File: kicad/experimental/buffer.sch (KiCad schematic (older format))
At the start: 25 parts

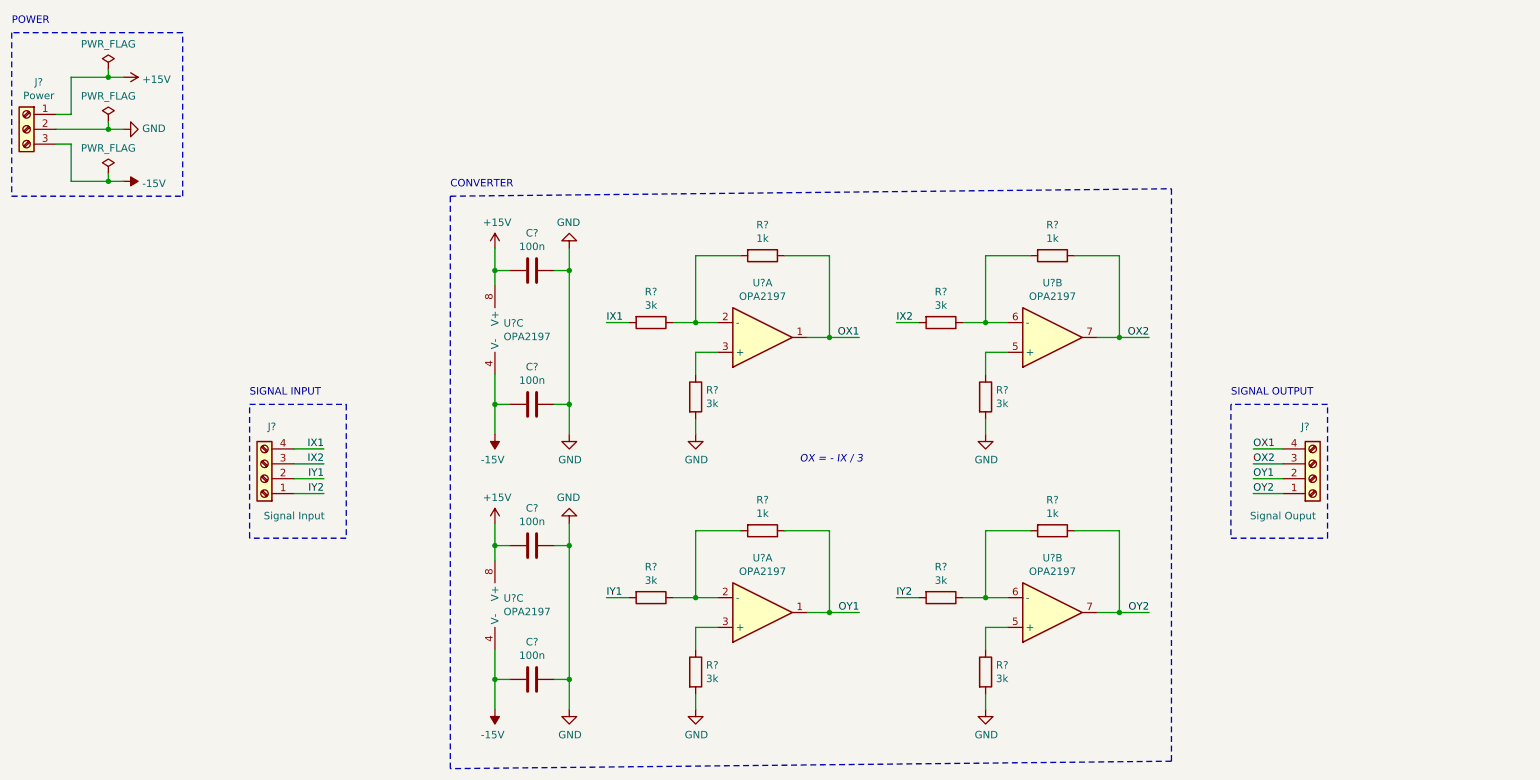
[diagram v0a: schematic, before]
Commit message: created schematic for experimental adc
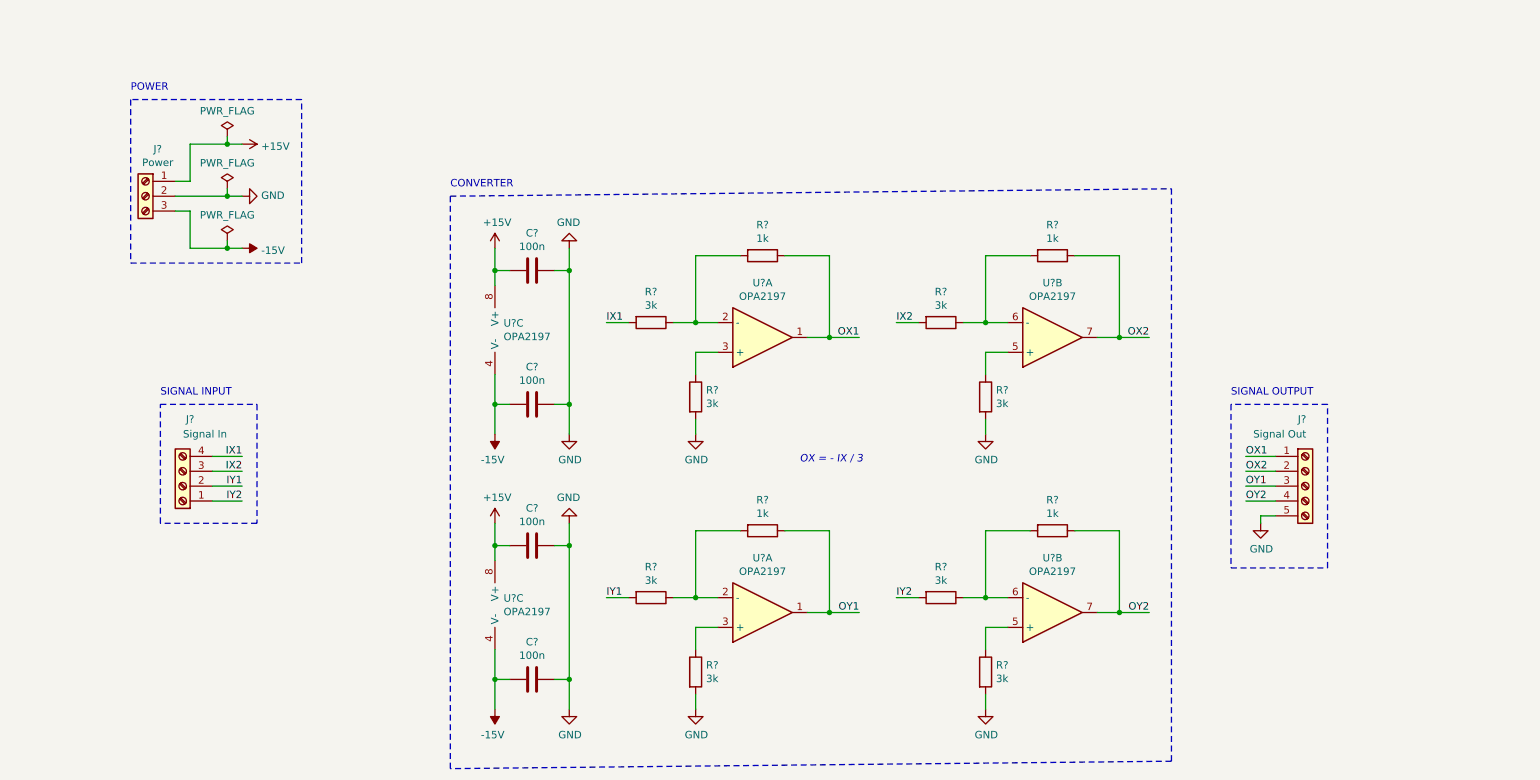
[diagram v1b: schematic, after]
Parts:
- removed J?: Signal Ouput, symbol Connector:Screw_Terminal_01x04
- added J?: Signal Out, symbol Connector:Screw_Terminal_01x05
- J?: value Signal Input -> Signal In
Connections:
- net GND: now also J?.5 (Pin_5)
- net OX1: now also J?.1 (Pin_1)
- net OX2: now also J?.2 (Pin_2)
- net OY1: now also J?.3 (Pin_3)
- net OY2: now also J?.4 (Pin_4)
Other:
- moved on the sheet: J?
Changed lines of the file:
@@
 L Connector:Screw_Terminal_01x03 J?
 U 1 1 5D6252EA
-P 850 1400
-F 0 "J?" H 768 1717 50  0000 C CNN
-F 1 "Power" H 768 1626 50  0000 C CNN
-F 2 "" H 850 1400 50  0001 C CNN
-F 3 "~" H 850 1400 50  0001 C CNN
-	1    850  1400
+P 1650 1850
+F 0 "J?" H 1568 2167 50  0000 C CNN
+F 1 "Power" H 1568 2076 50  0000 C CNN
+F 2 "" H 1650 1850 50  0001 C CNN
+F 3 "~" H 1650 1850 50  0001 C CNN
+	1    1650 1850
 	-1   0    0    -1
 $EndComp
@@
 L power:+15V #PWR?
 U 1 1 5D627080
-P 1500 1050
-F 0 "#PWR?" H 1500 900 50  0001 C CNN
-F 1 "+15V" V 1515 1178 50  0000 L CNN
-F 2 "" H 1500 1050 50  0001 C CNN
-F 3 "" H 1500 1050 50  0001 C CNN
-	1    1500 1050
-	0    1    1    0
-$EndComp
-Wire Wire Line
-	1500 1050 1400 1050
-Wire Wire Line
-	1150 1050 1150 1300
-Wire Wire Line
-	1150 1300 1050 1300
+P 2300 1500
+F 0 "#PWR?" H 2300 1350 50  0001 C CNN
+F 1 "+15V" V 2315 1628 50  0000 L CNN
+F 2 "" H 2300 1500 50  0001 C CNN
+F 3 "" H 2300 1500 50  0001 C CNN
+	1    2300 1500
+	0    1    1    0
+$EndComp
+Wire Wire Line
+	2300 1500 2200 1500
+Wire Wire Line
+	1950 1500 1950 1750
+Wire Wire Line
+	1950 1750 1850 1750
 $Comp
 L power:-15V #PWR?
 U 1 1 5D627AC9
-P 1500 1750
-F 0 "#PWR?" H 1500 1850 50  0001 C CNN
-F 1 "-15V" V 1515 1878 50  0000 L CNN
-F 2 "" H 1500 1750 50  0001 C CNN
-F 3 "" H 1500 1750 50  0001 C CNN
-	1    1500 1750
-	0    1    1    0
-$EndComp
-Wire Wire Line
-	1500 1750 1400 1750
-Wire Wire Line
-	1150 1750 1150 1500
-Wire Wire Line
-	1150 1500 1050 1500
+P 2300 2200
+F 0 "#PWR?" H 2300 2300 50  0001 C CNN
+F 1 "-15V" V 2315 2328 50  0000 L CNN
+F 2 "" H 2300 2200 50  0001 C CNN
+F 3 "" H 2300 2200 50  0001 C CNN
+	1    2300 2200
+	0    1    1    0
+$EndComp
+Wire Wire Line
+	2300 2200 2200 2200
+Wire Wire Line
+	1950 2200 1950 1950
+Wire Wire Line
+	1950 1950 1850 1950
 $Comp
 L power:GND #PWR?
 U 1 1 5D628485
-P 1500 1400
-F 0 "#PWR?" H 1500 1150 50  0001 C CNN
-F 1 "GND" V 1505 1272 50  0000 R CNN
-F 2 "" H 1500 1400 50  0001 C CNN
-F 3 "" H 1500 1400 50  0001 C CNN
-	1    1500 1400
+P 2300 1850
+F 0 "#PWR?" H 2300 1600 50  0001 C CNN
+F 1 "GND" V 2305 1722 50  0000 R CNN
+F 2 "" H 2300 1850 50  0001 C CNN
+F 3 "" H 2300 1850 50  0001 C CNN
+	1    2300 1850
 	0    -1   -1   0
 $EndComp
 Wire Wire Line
-	1500 1400 1400 1400
+	2300 1850 2200 1850
 $Comp
 L power:PWR_FLAG #FLG?
 U 1 1 5D628CB7
-P 1400 1000
-F 0 "#FLG?" H 1400 1075 50  0001 C CNN
-F 1 "PWR_FLAG" H 1400 1173 50  0000 C CNN
-F 2 "" H 1400 1000 50  0001 C CNN
-F 3 "~" H 1400 1000 50  0001 C CNN
-	1    1400 1000
-	1    0    0    -1
-$EndComp
-Wire Wire Line
-	1400 1000 1400 1050
-Connection ~ 1400 1050
-Wire Wire Line
-	1400 1050 1150 1050
+P 2200 1450
+F 0 "#FLG?" H 2200 1525 50  0001 C CNN
+F 1 "PWR_FLAG" H 2200 1623 50  0000 C CNN
+F 2 "" H 2200 1450 50  0001 C CNN
+F 3 "~" H 2200 1450 50  0001 C CNN
+	1    2200 1450
+	1    0    0    -1
+$EndComp
+Wire Wire Line
+	2200 1450 2200 1500
+Connection ~ 2200 1500
+Wire Wire Line
+	2200 1500 1950 1500
 $Comp
 L power:PWR_FLAG #FLG?
 U 1 1 5D62989E
-P 1400 1350
-F 0 "#FLG?" H 1400 1425 50  0001 C CNN
-F 1 "PWR_FLAG" H 1400 1523 50  0000 C CNN
-F 2 "" H 1400 1350 50  0001 C CNN
-F 3 "~" H 1400 1350 50  0001 C CNN
-	1    1400 1350
-	1    0    0    -1
-$EndComp
-Wire Wire Line
-	1400 1350 1400 1400
-Connection ~ 1400 1400
-Wire Wire Line
-	1400 1400 1050 1400
+P 2200 1800
+F 0 "#FLG?" H 2200 1875 50  0001 C CNN
+F 1 "PWR_FLAG" H 2200 1973 50  0000 C CNN
+F 2 "" H 2200 1800 50  0001 C CNN
+F 3 "~" H 2200 1800 50  0001 C CNN
+	1    2200 1800
+	1    0    0    -1
+$EndComp
+Wire Wire Line
+	2200 1800 2200 1850
+Connection ~ 2200 1850
+Wire Wire Line
+	2200 1850 1850 1850
 $Comp
 L power:PWR_FLAG #FLG?
 U 1 1 5D629BA8
-P 1400 1700
-F 0 "#FLG?" H 1400 1775 50  0001 C CNN
-F 1 "PWR_FLAG" H 1400 1873 50  0000 C CNN
-F 2 "" H 1400 1700 50  0001 C CNN
-F 3 "~" H 1400 1700 50  0001 C CNN
-	1    1400 1700
-	1    0    0    -1
-$EndComp
-Wire Wire Line
-	1400 1700 1400 1750
-Connection ~ 1400 1750
-Wire Wire Line
-	1400 1750 1150 1750
-Wire Notes Line
-	750  750  750  1850
-Wire Notes Line
-	750  1850 1900 1850
-Wire Notes Line
-	1900 1850 1900 750
-Wire Notes Line
-	1900 750  750  750
-Text Notes 750  700  0    50   ~ 0
+P 2200 2150
+F 0 "#FLG?" H 2200 2225 50  0001 C CNN
+F 1 "PWR_FLAG" H 2200 2323 50  0000 C CNN
+F 2 "" H 2200 2150 50  0001 C CNN
+F 3 "~" H 2200 2150 50  0001 C CNN
+	1    2200 2150
+	1    0    0    -1
+$EndComp
+Wire Wire Line
+	2200 2150 2200 2200
+Connection ~ 2200 2200
+Wire Wire Line
+	2200 2200 1950 2200
+Wire Notes Line
+	1550 1200 1550 2300
+Wire Notes Line
+	1550 2300 2700 2300
+Wire Notes Line
+	2700 2300 2700 1200
+Wire Notes Line
+	2700 1200 1550 1200
+Text Notes 1550 1150 0    50   ~ 0
 POWER
 $Comp
@@
 L Connector:Screw_Terminal_01x04 J?
 U 1 1 5D62F7ED
-P 2450 3750
-F 0 "J?" H 2400 3400 50  0000 C CNN
-F 1 "Signal Input" H 2250 4000 50  0000 C CNN
-F 2 "" H 2450 3750 50  0001 C CNN
-F 3 "~" H 2450 3750 50  0001 C CNN
-	1    2450 3750
+P 1900 3800
+F 0 "J?" H 1850 3350 50  0000 C CNN
+F 1 "Signal In" H 1750 3450 50  0000 C CNN
+F 2 "" H 1900 3800 50  0001 C CNN
+F 3 "~" H 1900 3800 50  0001 C CNN
+	1    1900 3800
 	-1   0    0    1
 $EndComp
-Text Label 2850 3550 2    50   ~ 0
+Text Label 2300 3600 2    50   ~ 0
 IX1
 Wire Wire Line
-	2850 3550 2650 3550
-Text Label 2850 3650 2    50   ~ 0
+	2300 3600 2100 3600
+Text Label 2300 3700 2    50   ~ 0
 IX2
 Wire Wire Line
-	2850 3650 2650 3650
-Text Label 2850 3750 2    50   ~ 0
+	2300 3700 2100 3700
+Text Label 2300 3800 2    50   ~ 0
 IY1
 Wire Wire Line
-	2850 3750 2650 3750
-Text Label 2850 3850 2    50   ~ 0
+	2300 3800 2100 3800
+Text Label 2300 3900 2    50   ~ 0
 IY2
 Wire Wire Line
-	2850 3850 2650 3850
-Wire Notes Line
-	2350 3250 3000 3250
-Wire Notes Line
-	3000 3250 3000 4150
-Wire Notes Line
-	3000 4150 2350 4150
-Wire Notes Line
-	2350 4150 2350 3250
-Text Notes 2350 3200 0    50   ~ 0
+	2300 3900 2100 3900
+Wire Notes Line
+	1750 3250 2400 3250
+Wire Notes Line
+	2400 3250 2400 4050
+Wire Notes Line
+	2400 4050 1750 4050
+Wire Notes Line
+	1750 4050 1750 3250
+Text Notes 1750 3200 0    50   ~ 0
 SIGNAL INPUT
 $Comp
@@
 Wire Wire Line
 	7150 4550 7300 4550
-$Comp
-L Connector:Screw_Terminal_01x04 J?
-U 1 1 5D6B2A8E
-P 9500 3750
-F 0 "J?" H 9450 3400 50  0000 C CNN
-F 1 "Signal Ouput" H 9300 4000 50  0000 C CNN
-F 2 "" H 9500 3750 50  0001 C CNN
-F 3 "~" H 9500 3750 50  0001 C CNN
-	1    9500 3750
-	1    0    0    1
-$EndComp
-Text Label 9100 3550 0    50   ~ 0
+Text Label 9050 3600 0    50   ~ 0
 OX1
 Wire Wire Line
-	9100 3550 9300 3550
-Text Label 9100 3650 0    50   ~ 0
+	9050 3600 9250 3600
+Text Label 9050 3700 0    50   ~ 0
 OX2
 Wire Wire Line
-	9100 3650 9300 3650
-Text Label 9100 3750 0    50   ~ 0
+	9050 3700 9250 3700
+Text Label 9050 3800 0    50   ~ 0
 OY1
 Wire Wire Line
-	9100 3750 9300 3750
-Text Label 9100 3850 0    50   ~ 0
+	9050 3800 9250 3800
+Text Label 9050 3900 0    50   ~ 0
 OY2
 Wire Wire Line
-	9100 3850 9300 3850
+	9050 3900 9250 3900
 Wire Notes Line
 	9600 3250 8950 3250
 Wire Notes Line
-	8950 3250 8950 4150
-Wire Notes Line
-	8950 4150 9600 4150
-Wire Notes Line
-	9600 4150 9600 3250
+	8950 3250 8950 4350
+Wire Notes Line
+	8950 4350 9600 4350
+Wire Notes Line
+	9600 4350 9600 3250
 Text Notes 8950 3200 0    50   ~ 0
 SIGNAL OUTPUT
 Text Notes 6050 3650 0    50   Italic 0
 OX = - IX / 3
+$Comp
+L Connector:Screw_Terminal_01x05 J?
+U 1 1 5D6D5912
+P 9450 3800
+F 0 "J?" H 9400 4250 50  0000 L CNN
+F 1 "Signal Out" H 9100 4150 50  0000 L CNN
+F 2 "" H 9450 3800 50  0001 C CNN
+F 3 "~" H 9450 3800 50  0001 C CNN
+	1    9450 3800
+	1    0    0    -1
+$EndComp
+$Comp
+L power:GND #PWR?
+U 1 1 5D6E01D6
+P 9150 4050
+F 0 "#PWR?" H 9150 3800 50  0001 C CNN
+F 1 "GND" H 9155 3877 50  0000 C CNN
+F 2 "" H 9150 4050 50  0001 C CNN
+F 3 "" H 9150 4050 50  0001 C CNN
+	1    9150 4050
+	1    0    0    -1
+$EndComp
+Wire Wire Line
+	9150 4050 9150 4000
+Wire Wire Line
+	9150 4000 9250 4000
 $EndSCHEMATC

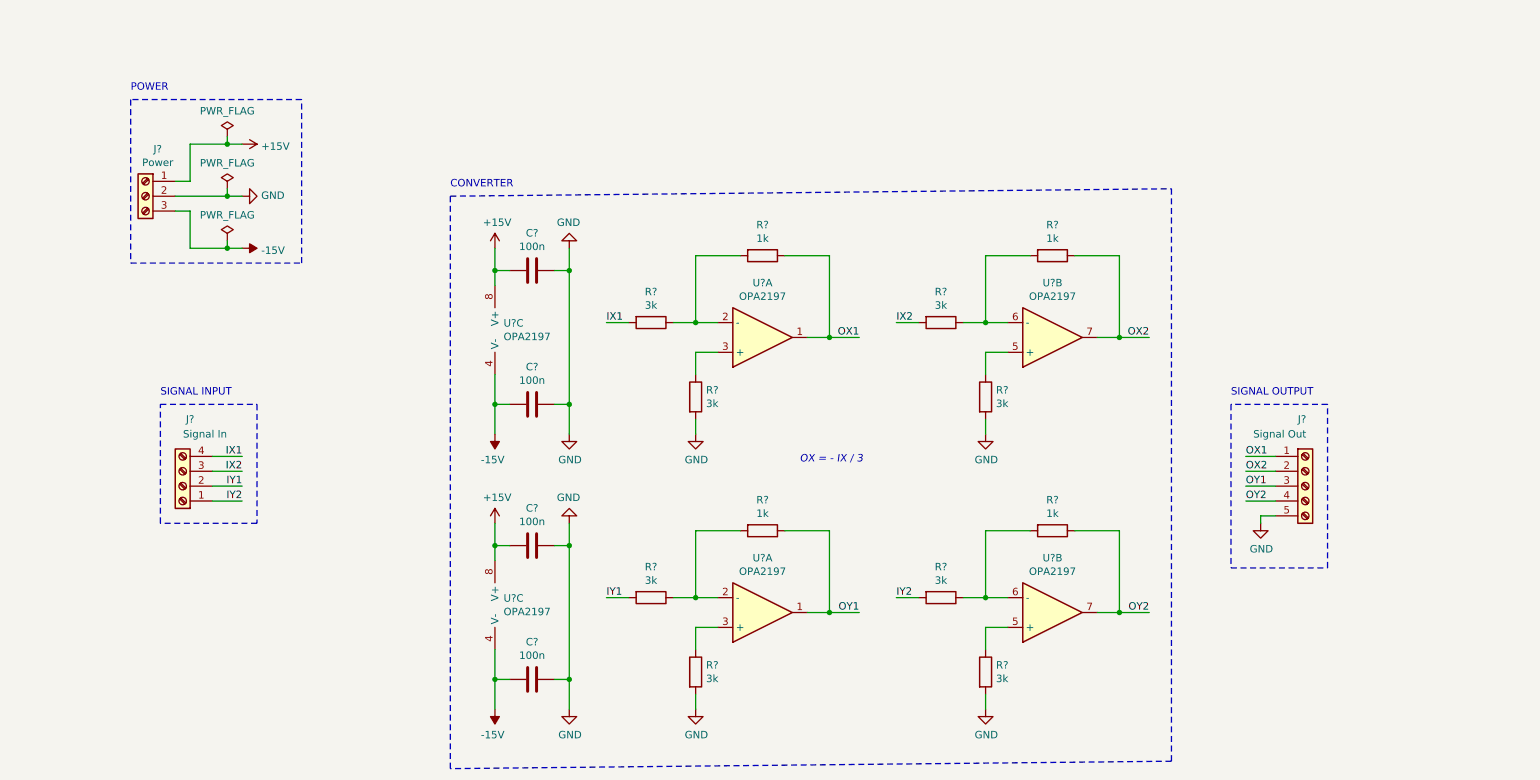
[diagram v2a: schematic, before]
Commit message: added test points to experimental adc and buffer boards, improved schematic, assigned footprints
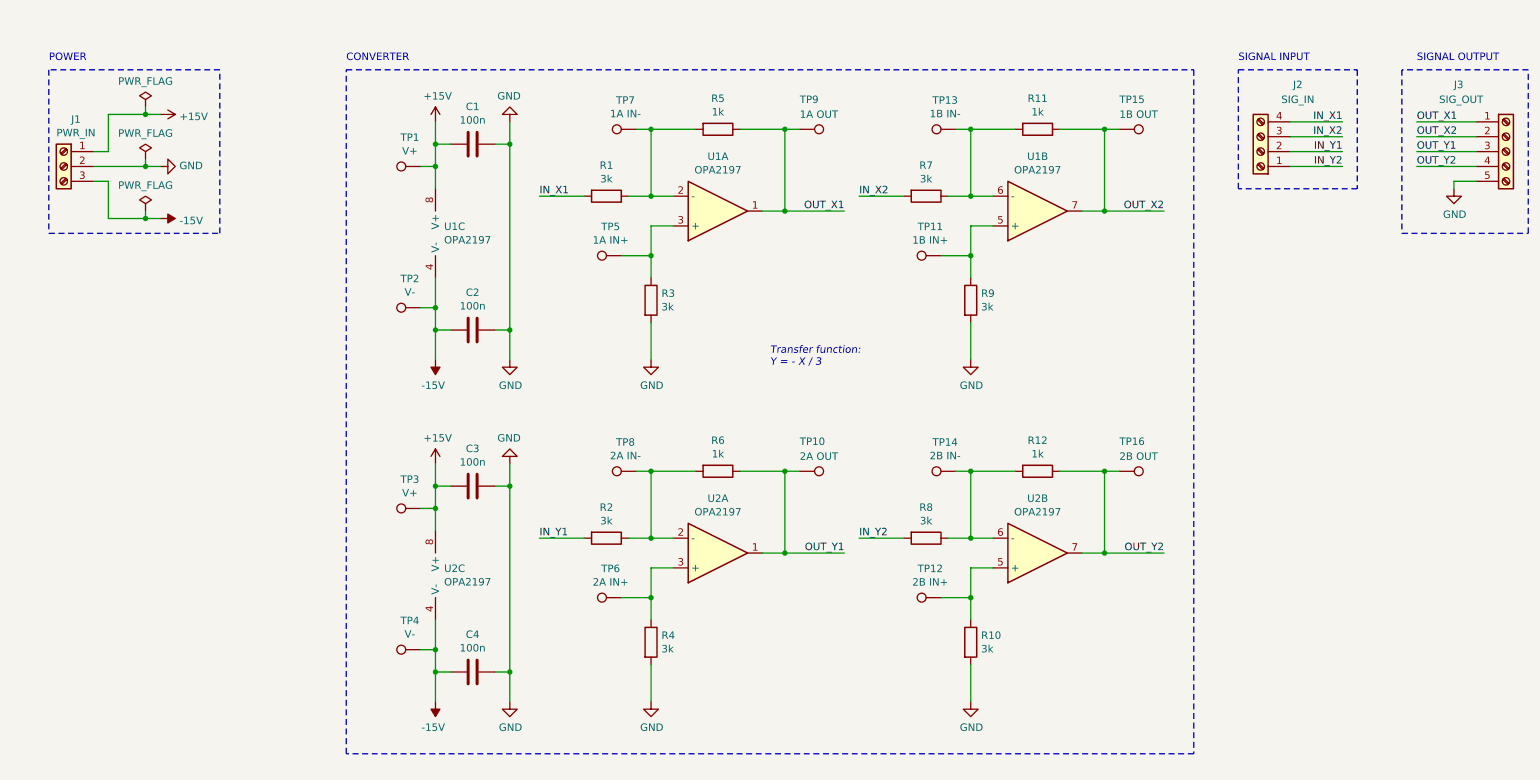
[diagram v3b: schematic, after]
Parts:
- removed C? (x2): 100n, symbol Device:C
- removed R? (x6): 3k, symbol Device:R
- removed R? (x3): 1k, symbol Device:R
- added C3, C4: 100n, Capacitor_SMD:C_0603_1608Metric, symbol Device:C
- added R10, R2, R4, R7, R8, R9: 3k, Resistor_SMD:R_0603_1608Metric, symbol Device:R
- added R11, R12, R6: 1k, Resistor_SMD:R_0603_1608Metric, symbol Device:R
- added TP1, TP3: V+, TestPoint:TestPoint_THTPad_1.0x1.0mm_Drill0.5mm, symbol Connector:TestPoint
- added TP10: 2A OUT, TestPoint:TestPoint_THTPad_1.0x1.0mm_Drill0.5mm, symbol Connector:TestPoint
- added TP11: 1B IN+, TestPoint:TestPoint_THTPad_1.0x1.0mm_Drill0.5mm, symbol Connector:TestPoint
- added TP12: 2B IN+, TestPoint:TestPoint_THTPad_1.0x1.0mm_Drill0.5mm, symbol Connector:TestPoint
- added TP13: 1B IN-, TestPoint:TestPoint_THTPad_1.0x1.0mm_Drill0.5mm, symbol Connector:TestPoint
- added TP14: 2B IN-, TestPoint:TestPoint_THTPad_1.0x1.0mm_Drill0.5mm, symbol Connector:TestPoint
- added TP15: 1B OUT, TestPoint:TestPoint_THTPad_1.0x1.0mm_Drill0.5mm, symbol Connector:TestPoint
- added TP16: 2B OUT, TestPoint:TestPoint_THTPad_1.0x1.0mm_Drill0.5mm, symbol Connector:TestPoint
- added TP2, TP4: V-, TestPoint:TestPoint_THTPad_1.0x1.0mm_Drill0.5mm, symbol Connector:TestPoint
- added TP5: 1A IN+, TestPoint:TestPoint_THTPad_1.0x1.0mm_Drill0.5mm, symbol Connector:TestPoint
- added TP6: 2A IN+, TestPoint:TestPoint_THTPad_1.0x1.0mm_Drill0.5mm, symbol Connector:TestPoint
- added TP7: 1A IN-, TestPoint:TestPoint_THTPad_1.0x1.0mm_Drill0.5mm, symbol Connector:TestPoint
- added TP8: 2A IN-, TestPoint:TestPoint_THTPad_1.0x1.0mm_Drill0.5mm, symbol Connector:TestPoint
- added TP9: 1A OUT, TestPoint:TestPoint_THTPad_1.0x1.0mm_Drill0.5mm, symbol Connector:TestPoint
- C1, C2: renamed from C?; footprint (none) -> Capacitor_SMD:C_0603_1608Metric
- J1: renamed from J?; value Power -> PWR_IN; footprint (none) -> TerminalBlock_TE-Connectivity:TerminalBlock_TE_282834-3_1x03_P2.54mm_Horizontal
- J2: renamed from J?; value Signal In -> SIG_IN; footprint (none) -> TerminalBlock_TE-Connectivity:TerminalBlock_TE_282834-4_1x04_P2.54mm_Horizontal
- J3: renamed from J?; value Signal Out -> SIG_OUT; footprint (none) -> TerminalBlock_TE-Connectivity:TerminalBlock_TE_282834-5_1x05_P2.54mm_Horizontal
- R1, R3, R5: renamed from R?; footprint (none) -> Resistor_SMD:R_0603_1608Metric
- U1, U2: renamed from U?; footprint (none) -> Package_SO:SOIC-8_3.9x4.9mm_P1.27mm
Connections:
- net +15V: now also C3.1, TP1.1, TP3.1
- net -15V: now also C4.1, TP2.1, TP4.1
- net GND: now also C3.2, C4.2, R10.2, R4.2, R9.2
- net at R1.1, R5.2, U1.2 (-): now also TP7.1
- net at R3.1, U1.3 (+): now also TP5.1
- net at U1.5 (+): now also R9.1, TP11.1
- net at U1.6 (-): now also R11.2, R7.1, TP13.1
- net at U2.2 (-): now also R2.1, R6.2, TP8.1
- net at U2.3 (+): now also R4.1, TP6.1
- net at U2.5 (+): now also R10.1, TP12.1
- net at U2.6 (-): now also R12.2, R8.1, TP14.1
- net IX1 renamed IN_X1
- net IX2 renamed IN_X2
- net IN_X2: now also R7.2
- net IY1 renamed IN_Y1
- net IN_Y1: now also R2.2
- net IY2 renamed IN_Y2
- net IN_Y2: now also R8.2
- net OX1 renamed OUT_X1
- net OUT_X1: now also TP9.1
- net OX2 renamed OUT_X2
- net OUT_X2: now also R11.1, TP15.1
- net OY1 renamed OUT_Y1
- net OUT_Y1: now also R6.1, TP10.1
- net OY2 renamed OUT_Y2
- net OUT_Y2: now also R12.1, TP16.1
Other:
- note added: "Transfer function:\nY = - X / 3"
- note removed: "OX = - IX / 3"
- moved on the sheet: C1, C2, J1, J2, J3, R1, R3, R5, U1A, U1B, U1C, U2A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
